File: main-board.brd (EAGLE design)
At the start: 49.2 x 17.8 mm, 53 parts, among them IC1 MEGA328-PB, IC2 MCP73831, IC3 LE33, Q1 3,6864 MHz, Q4 TSM2302CX, T1 IRF7306

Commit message: Optimize for BOM.
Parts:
- C1, C2: value 22pF -> 22p
- C3, C7: value 100nF -> 100n
- C4: value 10nF -> 10n
- CON-BT-POWER, CON-DEBUG: value (none) -> PINHEAD
- R10: value 100k -> 100K
- R13, R6: value 10k -> 10K
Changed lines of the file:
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@@
 </autorouter>
 <elements>
-<element name="C1" library="rcl" package="C0805" value="22pF" x="26.3525" y="6.0325" smashed="yes">
+<element name="C1" library="rcl" package="C0805" value="22p" x="26.3525" y="6.0325" smashed="yes">
 <attribute name="NAME" x="26.9875" y="5.08" size="1.016" layer="25" rot="R90"/>
 <attribute name="VALUE" x="25.0825" y="3.4925" size="1.27" layer="27"/>
@@
 <attribute name="VALUE" x="45.085" y="4.445" size="1.27" layer="28" rot="MR270"/>
 </element>
-<element name="C2" library="rcl" package="C0805" value="22pF" x="27.305" y="4.1275" smashed="yes" rot="R180">
+<element name="C2" library="rcl" package="C0805" value="22p" x="27.305" y="4.1275" smashed="yes" rot="R180">
 <attribute name="NAME" x="26.67" y="5.08" size="1.27" layer="25" rot="R270"/>
 <attribute name="VALUE" x="28.575" y="6.6675" size="1.27" layer="27" rot="R180"/>
 </element>
-<element name="C3" library="rcl" package="C0805" value="100nF" x="23.8125" y="5.08" smashed="yes" rot="MR270">
+<element name="C3" library="rcl" package="C0805" value="100n" x="23.8125" y="5.08" smashed="yes" rot="MR270">
 <attribute name="NAME" x="22.86" y="5.715" size="1.016" layer="26" rot="MR270"/>
 <attribute name="VALUE" x="26.3525" y="6.35" size="1.27" layer="28" rot="MR270"/>
 </element>
-<element name="C4" library="rcl" package="C0805" value="10nF" x="21.59" y="10.4775" smashed="yes" rot="MR180">
+<element name="C4" library="rcl" package="C0805" value="10n" x="21.59" y="10.4775" smashed="yes" rot="MR180">
 <attribute name="NAME" x="20.6375" y="9.525" size="1.016" layer="26" rot="MR180"/>
 <attribute name="VALUE" x="20.32" y="13.0175" size="1.27" layer="28" rot="MR180"/>
@@
 <attribute name="VALUE" x="30.7975" y="6.35" size="1.27" layer="28" rot="MR270"/>
 </element>
-<element name="C7" library="rcl" package="C0805" value="100nF" x="34.29" y="9.2075" smashed="yes" rot="MR90">
+<element name="C7" library="rcl" package="C0805" value="100n" x="34.29" y="9.2075" smashed="yes" rot="MR90">
 <attribute name="NAME" x="35.2425" y="10.795" size="1.016" layer="26" rot="MR0"/>
 <attribute name="VALUE" x="31.75" y="7.9375" size="1.27" layer="28" rot="MR90"/>
@@
 <attribute name="VALUE" x="5.3975" y="1.27" size="1.27" layer="27" rot="R90"/>
 </element>
-<element name="CON-BT-POWER" library="pinhead" package="1X03" value="" x="5.715" y="12.7" smashed="yes" rot="R270">
+<element name="CON-BT-POWER" library="pinhead" package="1X03" value="PINHEAD" x="5.715" y="12.7" smashed="yes" rot="R270">
 <attribute name="VALUE" x="2.54" y="16.51" size="1.27" layer="27" rot="R270"/>
 </element>
-<element name="CON-DEBUG" library="pinhead" package="1X04" value="" x="18.7325" y="14.2875" smashed="yes" rot="R180">
+<element name="CON-DEBUG" library="pinhead" package="1X04" value="PINHEAD" x="18.7325" y="14.2875" smashed="yes" rot="R180">
 <attribute name="VALUE" x="23.8125" y="17.4625" size="1.27" layer="27" rot="R180"/>
 </element>
@@
 <attribute name="VALUE" x="11.7475" y="12.3825" size="1.27" layer="28" rot="MR0"/>
 </element>
-<element name="R10" library="rcl" package="R0805" value="100k" x="37.465" y="14.9225" smashed="yes" rot="MR270">
+<element name="R10" library="rcl" package="R0805" value="100K" x="37.465" y="14.9225" smashed="yes" rot="MR270">
 <attribute name="NAME" x="38.735" y="16.1925" size="1.016" layer="26" rot="MR0"/>
 <attribute name="VALUE" x="40.005" y="15.5575" size="1.27" layer="28" rot="MR270"/>
@@
 <attribute name="VALUE" x="32.385" y="15.5575" size="1.27" layer="28" rot="MR270"/>
 </element>
-<element name="R13" library="rcl" package="R0805" value="10k" x="31.75" y="14.9225" smashed="yes" rot="MR90">
+<element name="R13" library="rcl" package="R0805" value="10K" x="31.75" y="14.9225" smashed="yes" rot="MR90">
 <attribute name="NAME" x="33.02" y="12.3825" size="1.016" layer="26" rot="MR0"/>
 <attribute name="VALUE" x="29.21" y="14.2875" size="1.27" layer="28" rot="MR90"/>
@@
 <attribute name="VALUE" x="35.56" y="7.62" size="1.27" layer="27" rot="R180"/>
 </element>
-<element name="R6" library="rcl" package="R0805" value="10k" x="17.4625" y="6.0325" smashed="yes" rot="MR0">
+<element name="R6" library="rcl" package="R0805" value="10K" x="17.4625" y="6.0325" smashed="yes" rot="MR0">
 <attribute name="NAME" x="18.0975" y="6.985" size="1.016" layer="26" rot="MR0"/>
 <attribute name="VALUE" x="18.0975" y="3.4925" size="1.27" layer="28" rot="MR0"/>

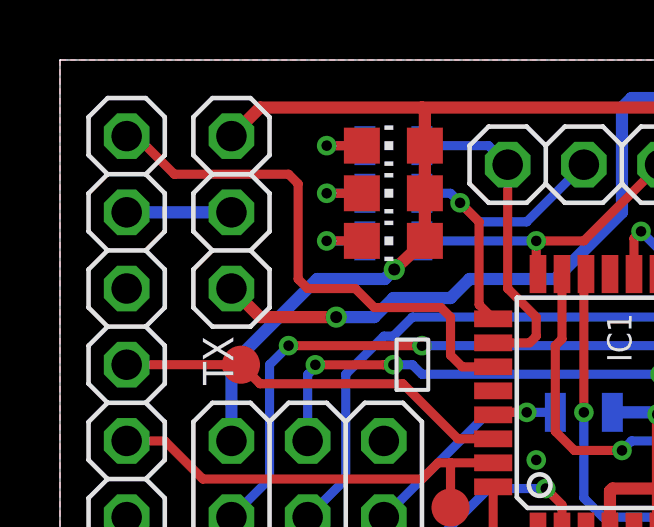
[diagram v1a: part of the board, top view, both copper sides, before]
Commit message: Con-bt-power -> jumper BT power.
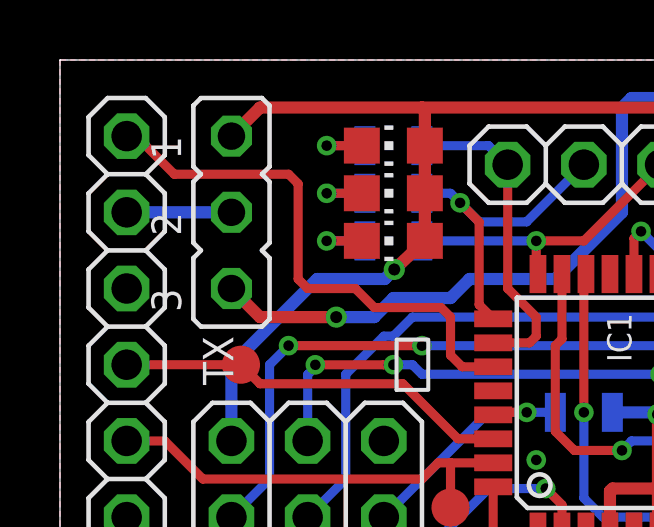
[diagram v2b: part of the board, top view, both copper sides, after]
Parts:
- removed CON-BT-POWER: PINHEAD, pinhead:1X03
- added JP-BT-POWER: PINHEAD, jumper:JP2
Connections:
- net BT-VCC: now also JP-BT-POWER.2; no longer CON-BT-POWER.2
- net VCC: now also JP-BT-POWER.1; no longer CON-BT-POWER.1
- net VCC-BAT: now also JP-BT-POWER.3; no longer CON-BT-POWER.3
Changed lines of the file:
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@@
 <attribute name="VALUE" x="5.3975" y="1.27" size="1.27" layer="27" rot="R90"/>
 </element>
-<element name="CON-BT-POWER" library="pinhead" package="1X03" value="PINHEAD" x="5.715" y="12.7" smashed="yes" rot="R270">
+<element name="JP-BT-POWER" library="jumper" package="JP2" value="PINHEAD" x="5.715" y="12.7" smashed="yes" rot="R270">
 <attribute name="VALUE" x="2.54" y="16.51" size="1.27" layer="27" rot="R270"/>
 </element>
@@
 <contactref element="R13" pad="1"/>
 <contactref element="R5" pad="2"/>
-<contactref element="CON-BT-POWER" pad="1"/>
+<contactref element="JP-BT-POWER" pad="1"/>
 <wire x1="31.75" y1="13.9725" x2="29.21" y2="11.4325" width="0.4064" layer="16"/>
 <wire x1="28.575" y1="7.62" x2="28.8925" y2="7.62" width="0.4064" layer="16"/>
@@
 <signal name="BT-VCC">
 <contactref element="CON-BT" pad="5"/>
-<contactref element="CON-BT-POWER" pad="2"/>
+<contactref element="JP-BT-POWER" pad="2"/>
 <wire x1="2.2225" y1="12.7" x2="5.715" y2="12.7" width="0.4064" layer="16"/>
 </signal>
@@
 <wire x1="38.3004" y1="7.1021" x2="38.735" y2="6.6675" width="0.4064" layer="1"/>
 <wire x1="34.6075" y1="6.665" x2="34.6075" y2="7.62" width="0.4064" layer="16"/>
-<contactref element="CON-BT-POWER" pad="3"/>
+<contactref element="JP-BT-POWER" pad="3"/>
 <wire x1="24.4475" y1="16.1925" x2="24.4475" y2="14.605" width="0.4064" layer="16"/>
 <wire x1="24.13" y1="16.51" x2="24.4475" y2="16.1925" width="0.4064" layer="16"/>

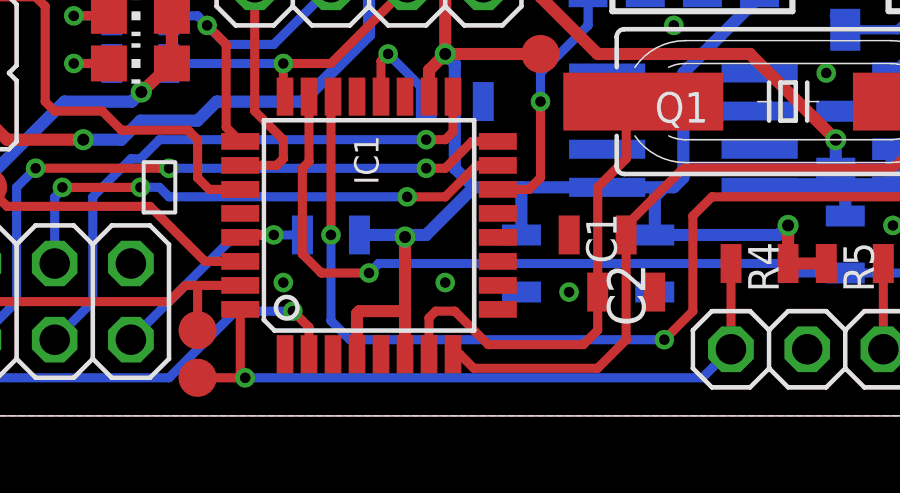
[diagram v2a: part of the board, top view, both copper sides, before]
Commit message: Connect OPTO-MEASURE to ICP (PB0).
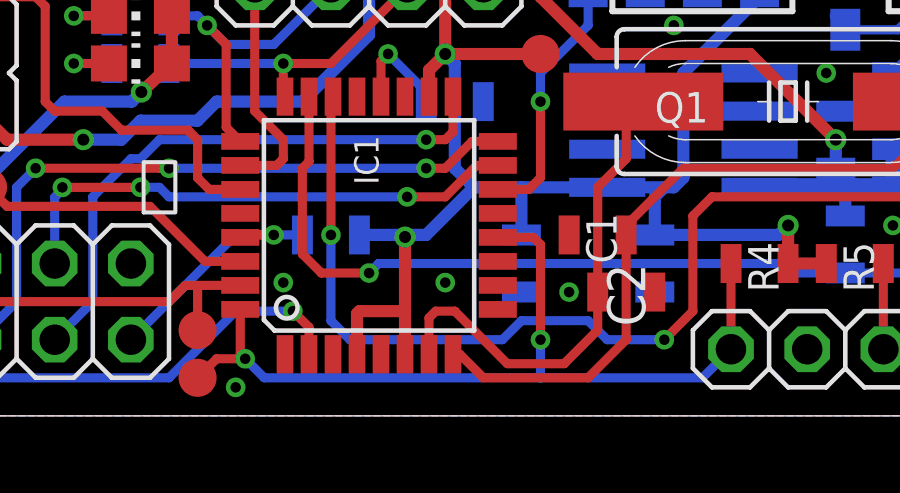
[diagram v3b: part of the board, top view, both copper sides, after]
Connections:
- net OPTO-MEASURE: now also IC1.12
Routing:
- net OPTO-MEASURE: track 23.4 -> 29.2 mm, vias 1 -> 2
- net CR2: track 15.8 -> 16.4 mm
- net CHARGE-STAT: track 40.6 -> 41.2 mm
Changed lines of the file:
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@@
 <contactref element="IC1" pad="8"/>
 <wire x1="21.5325" y1="2.0574" x2="21.7551" y2="2.0574" width="0.3048" layer="1"/>
-<wire x1="21.7551" y1="2.0574" x2="22.225" y2="1.5875" width="0.3048" layer="1"/>
-<wire x1="22.225" y1="1.5875" x2="26.3525" y2="1.5875" width="0.3048" layer="1"/>
-<wire x1="26.3525" y1="1.5875" x2="27.305" y2="2.54" width="0.3048" layer="1"/>
+<wire x1="21.7551" y1="2.0574" x2="22.5425" y2="1.27" width="0.3048" layer="1"/>
+<wire x1="22.5425" y1="1.27" x2="26.035" y2="1.27" width="0.3048" layer="1"/>
+<wire x1="26.035" y1="1.27" x2="27.305" y2="2.54" width="0.3048" layer="1"/>
 <wire x1="27.305" y1="2.54" x2="27.3025" y2="2.5425" width="0.3048" layer="1"/>
 <wire x1="27.3025" y1="2.5425" x2="27.3025" y2="6.0325" width="0.3048" layer="1"/>
@@
 <wire x1="26.355" y1="4.1275" x2="26.355" y2="7.6225" width="0.3048" layer="1"/>
 <wire x1="26.355" y1="7.6225" x2="27.305" y2="8.5725" width="0.3048" layer="1"/>
-<wire x1="26.355" y1="2.8575" x2="25.8724" y2="2.3749" width="0.3048" layer="1"/>
+<wire x1="26.355" y1="2.8575" x2="25.2374" y2="1.7399" width="0.3048" layer="1"/>
 <wire x1="26.355" y1="2.8575" x2="26.355" y2="4.1275" width="0.3048" layer="1"/>
 <contactref element="IC1" pad="7"/>
-<wire x1="25.8724" y1="2.3749" x2="22.7076" y2="2.3749" width="0.3048" layer="1"/>
-<wire x1="22.7076" y1="2.3749" x2="21.59" y2="3.4925" width="0.3048" layer="1"/>
+<wire x1="25.2374" y1="1.7399" x2="23.3426" y2="1.7399" width="0.3048" layer="1"/>
+<wire x1="23.3426" y1="1.7399" x2="21.59" y2="3.4925" width="0.3048" layer="1"/>
 <wire x1="21.59" y1="3.4925" x2="20.955" y2="3.4925" width="0.3048" layer="1"/>
 <wire x1="20.955" y1="3.4925" x2="20.7325" y2="3.27" width="0.3048" layer="1"/>
@@
 <via x="28.8925" y="13.0175" extent="1-16" drill="0.35"/>
 <via x="37.465" y="3.175" extent="1-16" drill="0.35"/>
+<via x="14.2875" y="0.9525" extent="1-16" drill="0.35"/>
 <wire x1="28.255" y1="4.1275" x2="28.2575" y2="4.13" width="0" layer="19" extent="1-16"/>
 </signal>
@@
 <wire x1="30.8" y1="5.08" x2="30.8" y2="2.225" width="0.3048" layer="1"/>
 <wire x1="30.8" y1="2.225" x2="30.7975" y2="2.2225" width="0.3048" layer="1"/>
-<wire x1="14.4399" y1="3.55" x2="14.4399" y2="1.4351" width="0.3048" layer="1"/>
-<wire x1="14.4399" y1="1.4351" x2="14.605" y2="1.27" width="0.3048" layer="1"/>
-<via x="14.605" y="1.27" extent="1-16" drill="0.35"/>
-<wire x1="14.605" y1="1.27" x2="29.845" y2="1.27" width="0.3048" layer="16"/>
+<wire x1="14.4399" y1="3.55" x2="14.4399" y2="2.0701" width="0.3048" layer="1"/>
+<wire x1="14.4399" y1="2.0701" x2="14.605" y2="1.905" width="0.3048" layer="1"/>
+<via x="14.605" y="1.905" extent="1-16" drill="0.35"/>
+<wire x1="14.605" y1="1.905" x2="15.24" y2="1.27" width="0.3048" layer="16"/>
+<wire x1="15.24" y1="1.27" x2="24.4475" y2="1.27" width="0.3048" layer="16"/>
+<wire x1="24.4475" y1="1.27" x2="29.845" y2="1.27" width="0.3048" layer="16"/>
 <wire x1="29.845" y1="1.27" x2="30.7975" y2="2.2225" width="0.3048" layer="16"/>
-<wire x1="13.0175" y1="1.27" x2="14.605" y2="1.27" width="0.3048" layer="1"/>
+<contactref element="IC1" pad="12"/>
+<wire x1="23.0251" y1="5.95" x2="24.2125" y2="5.95" width="0.3048" layer="1"/>
+<wire x1="24.2125" y1="5.95" x2="24.4475" y2="5.715" width="0.3048" layer="1"/>
+<wire x1="24.4475" y1="5.715" x2="24.4475" y2="2.54" width="0.3048" layer="1"/>
+<via x="24.4475" y="2.54" extent="1-16" drill="0.35"/>
+<wire x1="24.4475" y1="2.54" x2="24.4475" y2="1.27" width="0.3048" layer="16"/>
+<wire x1="14.605" y1="1.905" x2="13.6525" y2="1.905" width="0.3048" layer="1"/>
+<wire x1="13.6525" y1="1.905" x2="13.0175" y2="1.27" width="0.3048" layer="1"/>
 </signal>
 <signal name="MISO">
@@
 <wire x1="18.0975" y1="2.54" x2="17.4625" y2="3.175" width="0.3048" layer="16"/>
 <wire x1="17.4625" y1="3.175" x2="17.4625" y2="6.0325" width="0.3048" layer="16"/>
-<wire x1="28.575" y1="2.54" x2="18.0975" y2="2.54" width="0.3048" layer="16"/>
 <via x="17.4625" y="6.0325" extent="1-16" drill="0.35"/>
 <wire x1="17.5325" y1="10.6426" x2="17.4625" y2="10.5726" width="0.3048" layer="1"/>
@@
 <wire x1="40.9575" y1="3.175" x2="40.9575" y2="2.5125" width="0.3048" layer="1"/>
 <wire x1="40.9575" y1="2.5125" x2="41.595" y2="1.875" width="0.3048" layer="1"/>
+<wire x1="28.575" y1="2.54" x2="26.67" y2="2.54" width="0.3048" layer="16"/>
+<wire x1="26.67" y1="2.54" x2="26.035" y2="3.175" width="0.3048" layer="16"/>
+<wire x1="26.035" y1="3.175" x2="23.8125" y2="3.175" width="0.3048" layer="16"/>
+<wire x1="23.8125" y1="3.175" x2="23.1775" y2="2.54" width="0.3048" layer="16"/>
+<wire x1="23.1775" y1="2.54" x2="18.0975" y2="2.54" width="0.3048" layer="16"/>
 </signal>
 <signal name="CHARGE-STAT-LED">

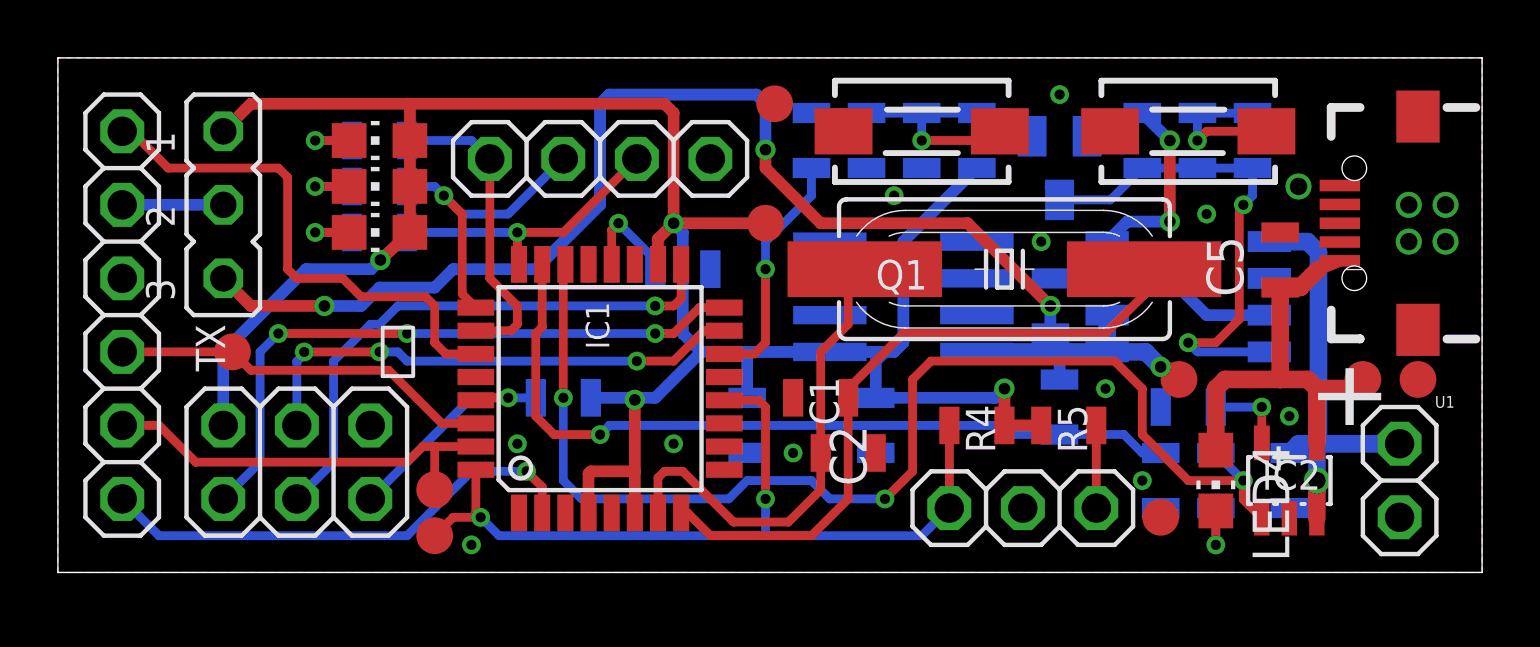
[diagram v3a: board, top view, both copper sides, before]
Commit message: Move CHARGE-STAT to digital pin.
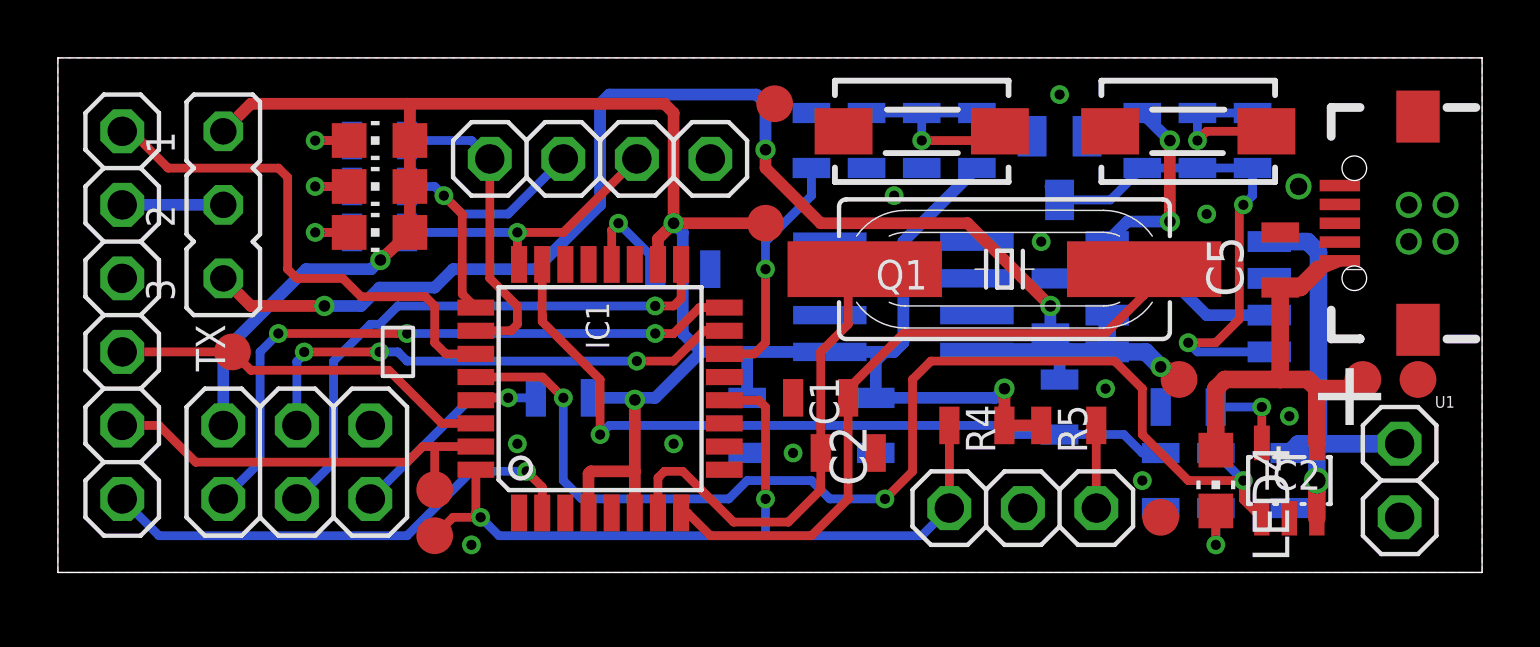
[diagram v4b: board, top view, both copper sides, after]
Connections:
- net CHARGE-STAT: now also IC1.28; no longer IC1.22
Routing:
- net CHARGE-STAT: track 41.2 -> 39.8 mm
- net BAT-SENSE: track 27.7 -> 26.6 mm
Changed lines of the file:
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@@
 <wire x1="33.0175" y1="4.765" x2="32.7025" y2="5.08" width="0.3048" layer="16"/>
 <via x="18.7325" y="4.7625" extent="1-16" drill="0.35"/>
-<wire x1="18.7325" y1="4.7625" x2="17.145" y2="4.7625" width="0.3048" layer="1"/>
-<wire x1="16.51" y1="5.3975" x2="17.145" y2="4.7625" width="0.3048" layer="1"/>
-<wire x1="16.7325" y1="10.6426" x2="16.7325" y2="8.4775" width="0.3048" layer="1"/>
-<wire x1="16.7325" y1="8.4775" x2="16.51" y2="8.255" width="0.3048" layer="1"/>
-<wire x1="16.51" y1="8.255" x2="16.51" y2="5.3975" width="0.3048" layer="1"/>
+<wire x1="18.7325" y1="6.6675" x2="18.7325" y2="4.7625" width="0.3048" layer="1"/>
+<wire x1="16.7325" y1="10.6426" x2="16.7325" y2="8.89" width="0.3048" layer="1"/>
+<wire x1="16.7325" y1="8.89" x2="16.7325" y2="8.795" width="0.3048" layer="1"/>
 <wire x1="32.7025" y1="5.08" x2="19.05" y2="5.08" width="0.3048" layer="16"/>
 <wire x1="19.05" y1="5.08" x2="18.7325" y2="4.7625" width="0.3048" layer="16"/>
 <wire x1="37.4675" y1="4.125" x2="38.1" y2="4.125" width="0.3048" layer="16"/>
+<wire x1="16.7325" y1="8.795" x2="16.7325" y2="8.6675" width="0.3048" layer="1"/>
+<wire x1="16.7325" y1="8.6675" x2="18.7325" y2="6.6675" width="0.3048" layer="1"/>
 </signal>
 <signal name="CPU-REF">
@@
 <contactref element="IC2" pad="1"/>
 <contactref element="R14" pad="1"/>
-<contactref element="IC1" pad="22"/>
 <via x="40.9575" y="3.175" extent="1-16" drill="0.35"/>
 <wire x1="40.9575" y1="3.175" x2="39.0525" y2="3.175" width="0.3048" layer="1"/>
@@
 <wire x1="17.4625" y1="3.175" x2="17.4625" y2="6.0325" width="0.3048" layer="16"/>
 <via x="17.4625" y="6.0325" extent="1-16" drill="0.35"/>
-<wire x1="17.5325" y1="10.6426" x2="17.4625" y2="10.5726" width="0.3048" layer="1"/>
-<wire x1="17.4625" y1="10.5726" x2="17.4625" y2="6.0325" width="0.3048" layer="1"/>
 <wire x1="40.9575" y1="3.175" x2="40.0075" y2="4.125" width="0.3048" layer="16"/>
 <wire x1="40.0075" y1="4.125" x2="40.005" y2="4.125" width="0.3048" layer="16"/>
@@
 <wire x1="23.8125" y1="3.175" x2="23.1775" y2="2.54" width="0.3048" layer="16"/>
 <wire x1="23.1775" y1="2.54" x2="18.0975" y2="2.54" width="0.3048" layer="16"/>
+<contactref element="IC1" pad="28"/>
+<wire x1="14.4399" y1="6.75" x2="16.745" y2="6.75" width="0.3048" layer="1"/>
+<wire x1="16.745" y1="6.75" x2="17.4625" y2="6.0325" width="0.3048" layer="1"/>
 </signal>
 <signal name="CHARGE-STAT-LED">
